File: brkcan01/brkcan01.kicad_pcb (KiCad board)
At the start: 2 copper layers, 16.5 x 12.1 mm, 3 parts, among them J1 Conn_01x04, J2 Conn_01x04, U1 SN65HVD232

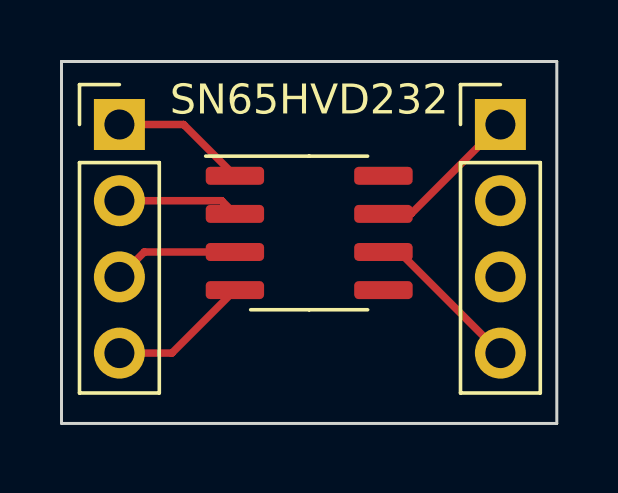
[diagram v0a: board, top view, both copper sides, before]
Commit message: Updates to CAN breakout
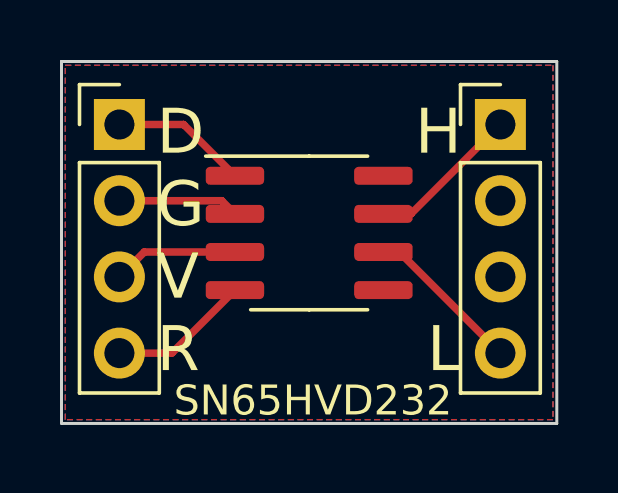
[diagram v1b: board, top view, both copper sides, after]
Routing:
- added copper zone on B.Cu, net (none)
- added copper zone on F.Cu, net (none)
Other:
- board text added: "CAN-3.3V nnarain"
- board text added: "D G V R"
- board text added: "H L"
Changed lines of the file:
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@@
       (effects (font (size 1 1) (thickness 0.15)))
     )
-    (fp_text value "SN65HVD232" (at 0 -4.445) (layer "F.SilkS")
+    (fp_text value "SN65HVD232" (at 0.127 5.588) (layer "F.SilkS")
       (effects (font (size 1 1) (thickness 0.15)))
     )
@@
   (gr_line (start 128.905 88.9) (end 128.905 100.965) (layer "Edge.Cuts") (width 0.1))
   (gr_line (start 112.395 100.965) (end 112.395 88.9) (layer "Edge.Cuts") (width 0.1))
+  (gr_text "CAN-3.3V\nnnarain" (at 120.523 94.869 90) (layer "B.SilkS")
+    (effects (font (size 1.5 1.5) (thickness 0.3)) (justify mirror))
+  )
+  (gr_text "H\n\n\nL" (at 125.73 94.869) (layer "F.SilkS")
+    (effects (font (size 1.5 1.5) (thickness 0.3)) (justify right))
+  )
+  (gr_text "D\nG\nV\nR" (at 115.57 94.869) (layer "F.SilkS")
+    (effects (font (size 1.5 1.5) (thickness 0.3)) (justify left))
+  )
   (segment (start 114.325 93.54) (end 117.735 93.54) (width 0.25) (layer "F.Cu") (net 1))
   (segment (start 117.735 93.54) (end 118.175 93.98) (width 0.25) (layer "F.Cu") (net 1))
@@
   (segment (start 123.655 95.25) (end 127.025 98.62) (width 0.25) (layer "F.Cu") (net 10))
   (segment (start 123.125 95.25) (end 123.655 95.25) (width 0.25) (layer "F.Cu") (net 10))
+  (zone (net 0) (net_name "") (layer "F.Cu") (hatch edge 0.508)
+    (connect_pads (clearance 0.508))
+    (min_thickness 0.254) (filled_areas_thickness no)
+    (fill yes (thermal_gap 0.508) (thermal_bridge_width 0.508))
+    (polygon
+      (pts
+        (xy 128.778 100.838)
+        (xy 112.522 100.838)
+        (xy 112.522 89.027)
+        (xy 128.778 89.027)
+      )
+    )
+  )
+  (zone (net 0) (net_name "") (layer "B.Cu") (hatch edge 0.508)
+    (connect_pads (clearance 0.508))
+    (min_thickness 0.254) (filled_areas_thickness no)
+    (fill yes (thermal_gap 0.508) (thermal_bridge_width 0.508))
+    (polygon
+      (pts
+        (xy 128.778 100.838)
+        (xy 112.522 100.838)
+        (xy 112.522 89.027)
+        (xy 128.778 89.027)
+      )
+    )
+  )
 )
